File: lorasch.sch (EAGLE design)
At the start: 12 parts, among them M1 ARDUINO-NANO-3.0

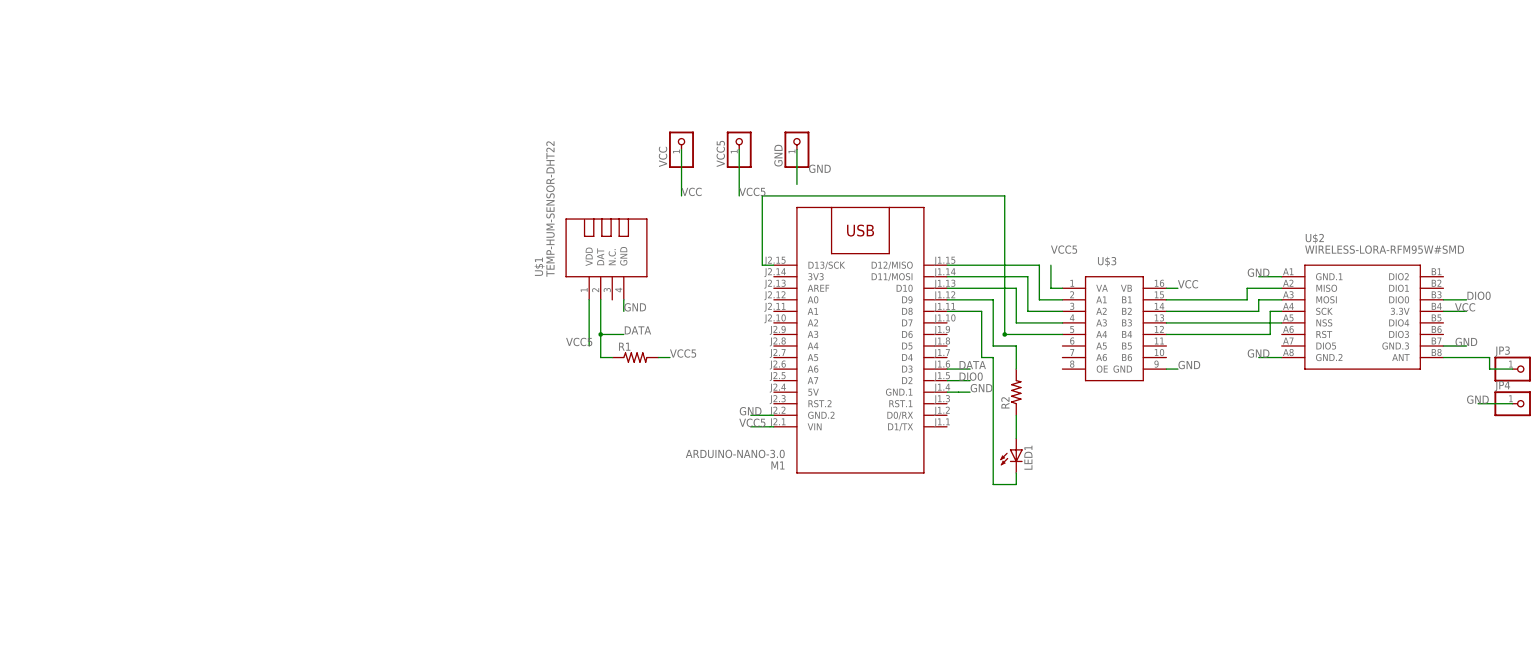
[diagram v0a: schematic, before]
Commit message: Modify schematic to reduce size of board.
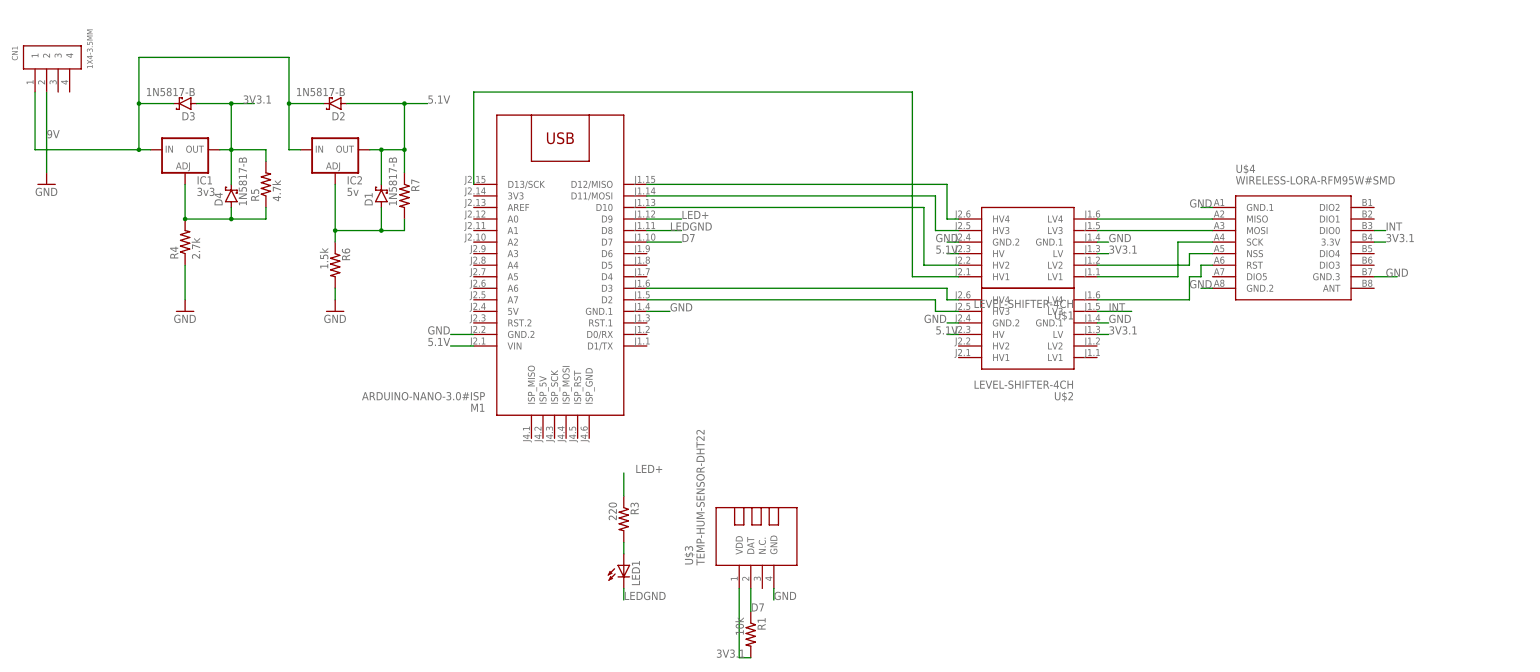
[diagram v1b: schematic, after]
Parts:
- removed GND, JP3, JP4, VCC, VCC5: (no value), adafruit:PINHD-1X1
- removed R2: (no value), adafruit:FLIPFLOP-RES
- added CN1: 1X4-3.5MM, adafruit:1X4-3.5MM
- added D1, D2, D3, D4: 1N5817-B, diode:1N5817-B
- added IC1: 3v3, v-reg:LM317TL
- added IC2: 5v, v-reg:LM317TL
- added R3: 220, adafruit:R-US_0204/7
- added R4: 2.7k, adafruit:R-US_0204/7
- added R5: 4.7k, adafruit:R-US_0204/7
- added R6: 1.5k, adafruit:R-US_0204/7
- added R7: (no value), adafruit:R-US_0204/7
- added U$4: WIRELESS-LORA-RFM95W#SMD, dht22:WIRELESS-LORA-RFM95W#SMD
- M1: value ARDUINO-NANO-3.0 -> ARDUINO-NANO-3.0#ISP; device dht22:ARDUINO-NANO-3.0 -> dht22:ARDUINO-NANO-3.0#ISP
- R1: value (none) -> 10k; device adafruit:FLIPFLOP-RES -> adafruit:R-US_0204/7
- U$1: value TEMP-HUM-SENSOR-DHT22 -> LEVEL-SHIFTER-4CH; device dht22:TEMP-HUM-SENSOR-DHT22 -> dht22:LEVEL-SHIFTER-4CH
- U$2: value WIRELESS-LORA-RFM95W#SMD -> LEVEL-SHIFTER-4CH; device dht22:WIRELESS-LORA-RFM95W#SMD -> dht22:LEVEL-SHIFTER-4CH
- U$3: value (none) -> TEMP-HUM-SENSOR-DHT22; device logicconv:TX50108E -> dht22:TEMP-HUM-SENSOR-DHT22
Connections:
- net N$8 renamed LEDGND
- removed net DATA: M1.D3, R1.1, U$1.DAT
- removed net DIO0: M1.D2, U$2.DIO0
- removed net N$10: U$2.NSS, U$3.B3
- removed net N$11: U$2.SCK, U$3.B4
- removed net N$12: U$2.MOSI, U$3.B2
- removed net VCC: U$2.3.3V, U$3.VB, VCC.1
- removed net VCC5: M1.VIN, R1.2, U$1.VDD, U$3.VA, VCC5.1
- new net 3V3.1: D3.A, D4.C, IC1.OUT, R1.2, R5.2, U$1.LV, U$2.LV, U$3.VDD, U$4.3.3V
- new net 5.1V: D1.C, D2.A, IC2.OUT, M1.VIN, R7.1, U$1.HV, U$2.HV
- new net 9V: CN1.1, D2.C, D3.C, IC1.IN, IC2.IN
- new net D7: M1.D7, R1.1, U$3.DAT
- new net INT: U$2.LV3, U$4.DIO0
- new net LED+: M1.D9, R3.1
- new net N$14: U$1.LV3, U$4.MOSI
- new net N$15: U$1.LV2, U$4.NSS
- new net N$16: U$1.LV1, U$4.SCK
- new net N$17: U$2.LV4, U$4.RST
- new net N$5: D1.A, IC2.ADJ, R6.1, R7.2
- new net N$8: M1.D11/MOSI, U$1.HV3
- net GND: now also CN1.2, R4.1, R6.2, U$1.GND.1, U$1.GND.2, U$4.GND.1, U$4.GND.2, U$4.GND.3; no longer GND.1, JP4.1, U$1.GND, U$2.GND.3
- net N$1: now also D4.A, IC1.ADJ, R4.2, R5.1; no longer M1.D12/MISO, U$3.A1
- net N$13: now also U$1.LV4, U$4.MISO; no longer U$2.MISO, U$3.B1
- net N$2: now also LED1.A, R3.2; no longer M1.D11/MOSI, U$3.A2
- net N$3: now also M1.D13/SCK, U$1.HV1; no longer M1.D10, U$3.A3
- net N$4: now also M1.D2, U$2.HV3; no longer M1.D13/SCK, U$3.A4
- net N$6: now also M1.D3, U$2.HV4; no longer M1.D9, R2.2
- net N$7: now also M1.D12/MISO, U$1.HV4; no longer LED1.A, R2.1
- net N$9: now also M1.D10, U$1.HV2; no longer JP3.1, U$2.ANT
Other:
- moved on the sheet: LED1, R1

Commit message: Connect all grounds to common plane.
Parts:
- added LSP1: SE14, solpad:SE14
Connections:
- new net N$10: LSP1.MP, U$4.ANT
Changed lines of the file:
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@@
 <part name="CN1" library="adafruit" library_urn="urn:adsk.eagle:library:420" deviceset="1X4" device="-3.5MM" package3d_urn="urn:adsk.eagle:package:6240819/1"/>
 <part name="GND3" library="supply1" library_urn="urn:adsk.eagle:library:371" deviceset="GND" device=""/>
+<part name="LSP1" library="solpad" library_urn="urn:adsk.eagle:library:364" deviceset="SE14" device="" package3d_urn="urn:adsk.eagle:package:26504/1"/>
 </parts>
 <sheets>
@@
 <instance part="GND3" gate="1" x="-152.4" y="83.82" smashed="yes">
 <attribute name="VALUE" x="-154.94" y="81.28" size="1.778" layer="96"/>
+</instance>
+<instance part="LSP1" gate="1" x="147.32" y="50.8" smashed="yes">
+<attribute name="NAME" x="146.05" y="53.721" size="1.778" layer="95"/>
 </instance>
 </instances>
@@
 </segment>
 </net>
+<net name="N$10" class="0">
+<segment>
+<pinref part="LSP1" gate="1" pin="MP"/>
+<pinref part="U$4" gate="G$1" pin="ANT"/>
+<wire x1="147.32" y1="48.26" x2="139.7" y2="48.26" width="0.1524" layer="91"/>
+<wire x1="139.7" y1="48.26" x2="139.7" y2="60.96" width="0.1524" layer="91"/>
+</segment>
+</net>

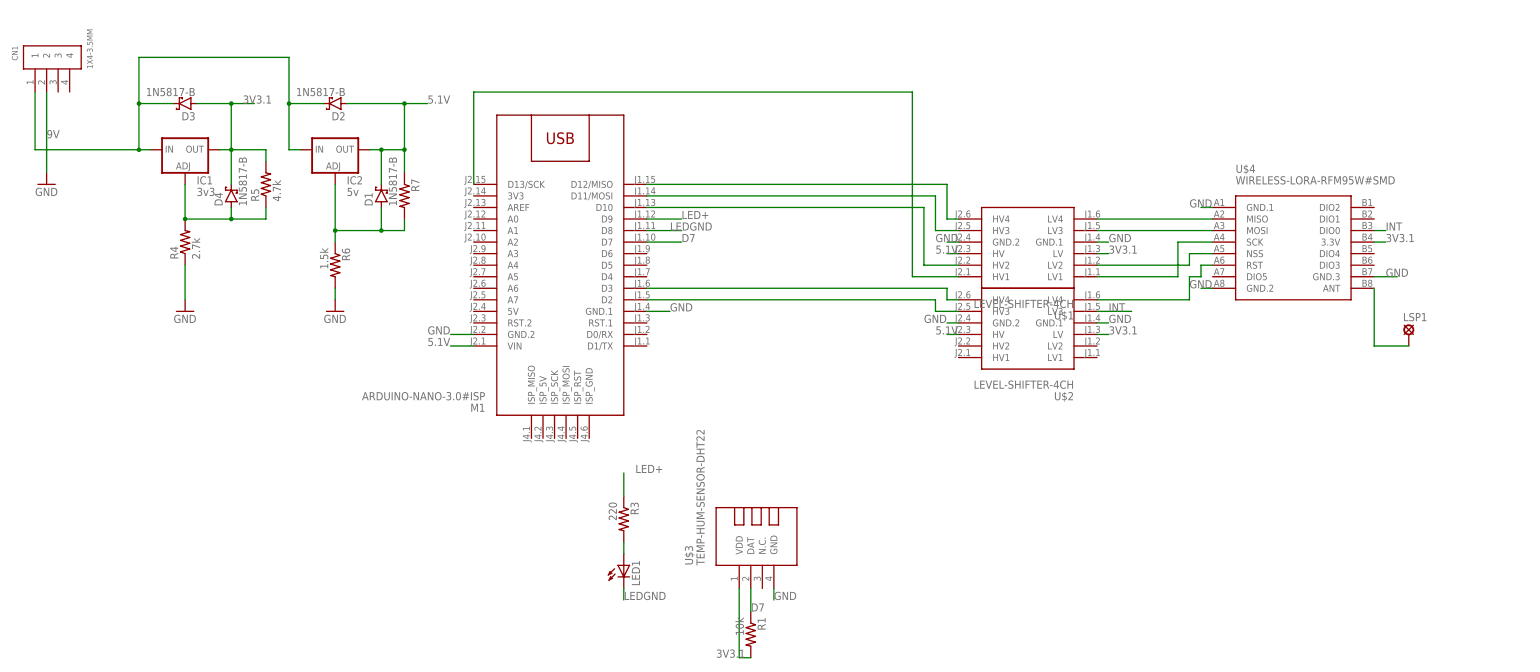
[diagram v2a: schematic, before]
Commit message: Add arduino pro mini 5v.
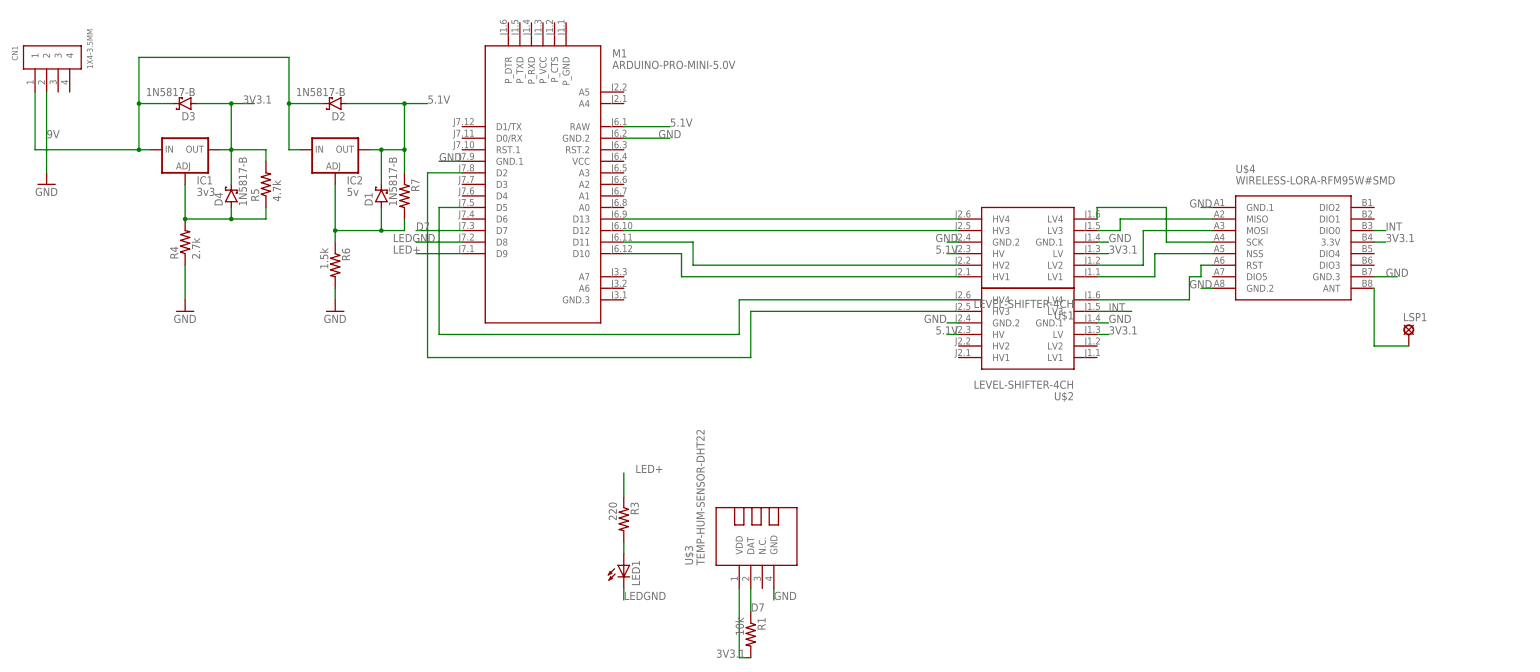
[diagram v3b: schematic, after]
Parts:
- M1: value ARDUINO-NANO-3.0#ISP -> ARDUINO-PRO-MINI-5.0V; device dht22:ARDUINO-NANO-3.0#ISP -> dht22:ARDUINO-PRO-MINI-5.0V
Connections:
- removed net N$16: U$1.LV1, U$4.SCK
- removed net N$6: M1.D3, U$2.HV4
- removed net N$9 (its old number): M1.D10, U$1.HV2
- new net N$11: U$1.LV2, U$4.MOSI
- new net N$12: U$1.LV3, U$4.MISO
- new net N$4: M1.D11, U$1.HV2
- net 5.1V: now also M1.RAW; no longer M1.VIN
- net N$13: now also U$4.SCK; no longer U$4.MISO
- net N$14: now also M1.D13, U$1.HV4; no longer U$1.LV3, U$4.MOSI
- net N$15: now also U$1.LV1; no longer U$1.LV2
- net N$3: now also M1.D12, U$1.HV3; no longer M1.D13/SCK, U$1.HV1
- net N$7: now also M1.D10, U$1.HV1; no longer M1.D12/MISO, U$1.HV4
- net N$8: now also M1.D5, U$2.HV4; no longer M1.D11/MOSI, U$1.HV3
